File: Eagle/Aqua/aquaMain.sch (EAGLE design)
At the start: 41 parts, among them IC1 ATMEGA168-20P, IC2 DS1307, IC3 74HC125N, IC4 L7805CV, IC5 LF33CV, IC6 PCF8574P, IC7 24LC256P, IC8 40106N, J1 POWER_JACKSLT, T1 BC337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

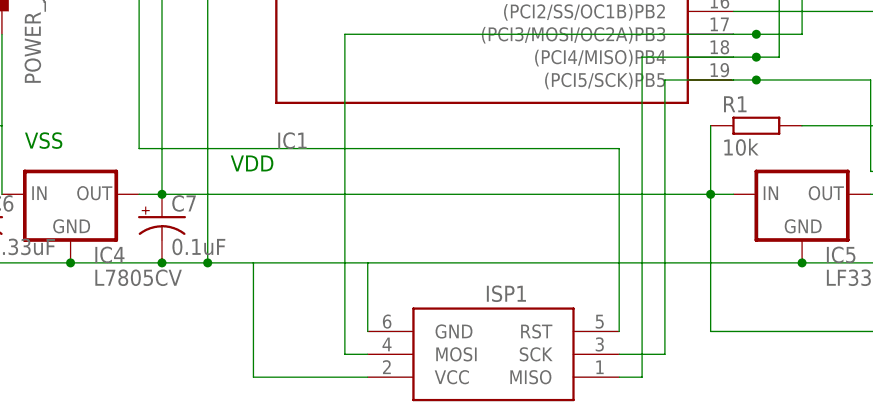
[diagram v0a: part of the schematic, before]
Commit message: Filled empty spaces with copper (faster eatching) Redone ArduinoNANO to DIP28 PCB to a single-side version Added V1 printout image
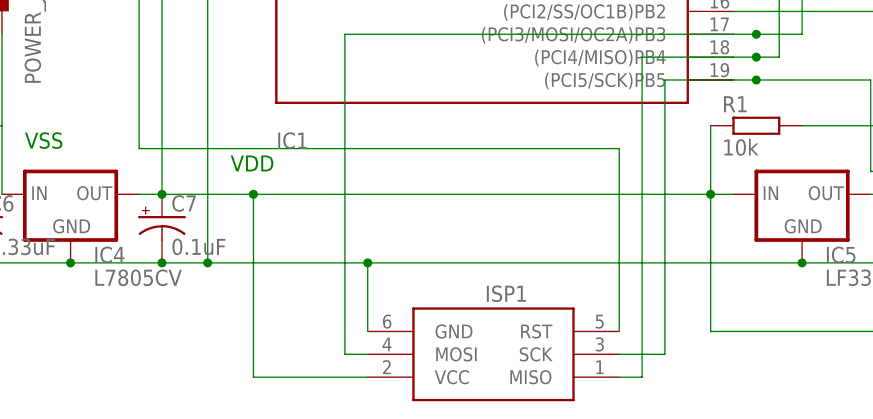
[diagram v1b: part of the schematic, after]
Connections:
- net N$25: now also ISP1.VCC
- net VSS: no longer ISP1.VCC
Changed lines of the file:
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@@
 <junction x="187.96" y="106.68"/>
 <pinref part="IC5" gate="G$1" pin="IN"/>
-<wire x1="68.58" y1="12.7" x2="129.54" y2="12.7" width="0.1524" layer="91"/>
+<wire x1="68.58" y1="12.7" x2="78.74" y2="12.7" width="0.1524" layer="91"/>
 <junction x="68.58" y="12.7"/>
 <pinref part="R1" gate="G$1" pin="1"/>
+<wire x1="78.74" y1="12.7" x2="129.54" y2="12.7" width="0.1524" layer="91"/>
 <wire x1="129.54" y1="12.7" x2="132.08" y2="12.7" width="0.1524" layer="91"/>
 <wire x1="129.54" y1="20.32" x2="129.54" y2="12.7" width="0.1524" layer="91"/>
@@
 <junction x="149.86" y="106.68"/>
 <pinref part="C7" gate="G$1" pin="+"/>
+<pinref part="ISP1" gate="G$1" pin="VCC"/>
+<wire x1="91.44" y1="-7.62" x2="78.74" y2="-7.62" width="0.1524" layer="91"/>
+<wire x1="78.74" y1="-7.62" x2="78.74" y2="12.7" width="0.1524" layer="91"/>
+<junction x="78.74" y="12.7"/>
 </segment>
 </net>
@@
 <wire x1="154.94" y1="5.08" x2="139.7" y2="5.08" width="0.1524" layer="91"/>
 <wire x1="139.7" y1="5.08" x2="91.44" y2="5.08" width="0.1524" layer="91"/>
-<wire x1="91.44" y1="5.08" x2="78.74" y2="5.08" width="0.1524" layer="91"/>
-<wire x1="78.74" y1="5.08" x2="73.66" y2="5.08" width="0.1524" layer="91"/>
+<wire x1="91.44" y1="5.08" x2="73.66" y2="5.08" width="0.1524" layer="91"/>
 <wire x1="203.2" y1="22.86" x2="203.2" y2="5.08" width="0.1524" layer="91"/>
 <junction x="203.2" y="5.08"/>
@@
 <pinref part="ISP1" gate="G$1" pin="GND"/>
 <wire x1="91.44" y1="-2.54" x2="91.44" y2="5.08" width="0.1524" layer="91"/>
-<pinref part="ISP1" gate="G$1" pin="VCC"/>
-<wire x1="91.44" y1="-7.62" x2="78.74" y2="-7.62" width="0.1524" layer="91"/>
-<wire x1="78.74" y1="-7.62" x2="78.74" y2="5.08" width="0.1524" layer="91"/>
 <pinref part="R4" gate="1" pin="1"/>
 <wire x1="91.44" y1="144.78" x2="91.44" y2="142.24" width="0.1524" layer="91"/>
@@
 <pinref part="C8" gate="G$1" pin="-"/>
 <junction x="154.94" y="5.08"/>
-</segment>
-</net>
+<junction x="91.44" y="5.08"/>
+</segment>
+</net>

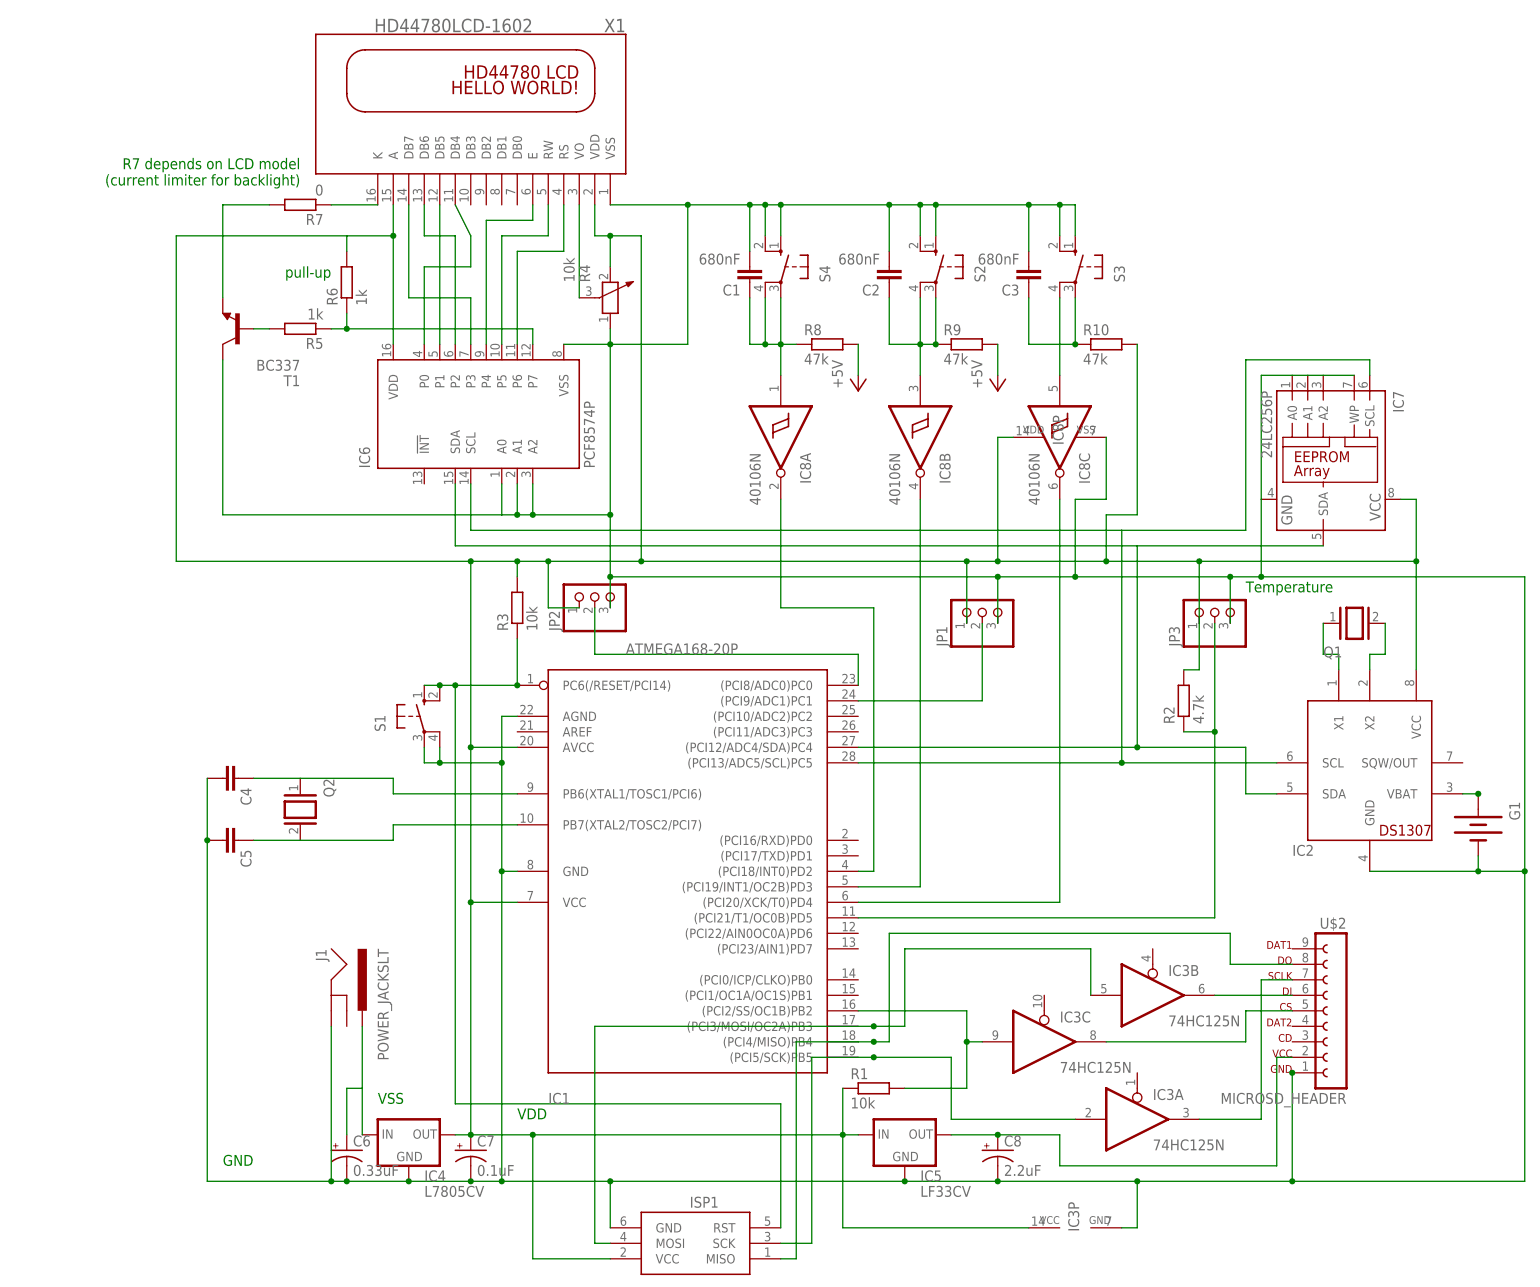
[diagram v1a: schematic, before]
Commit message: Big update Many important fixes dictated by 1st prototype
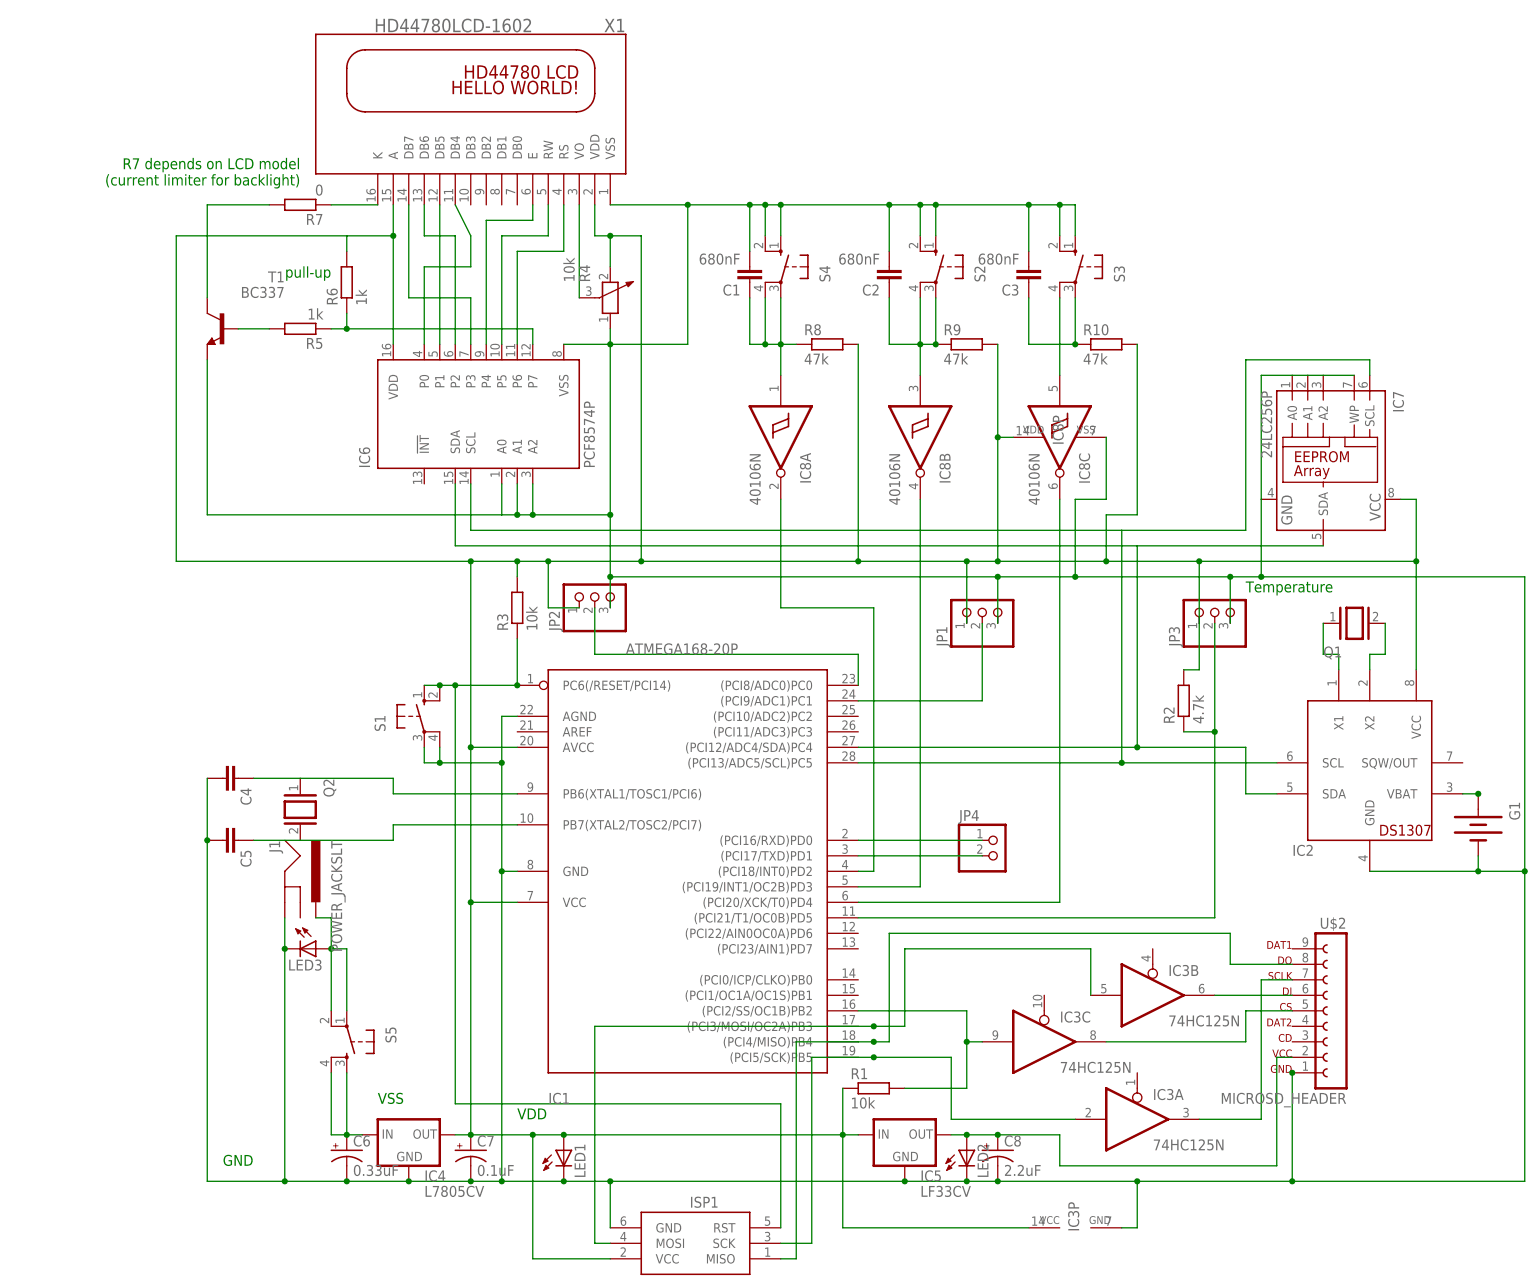
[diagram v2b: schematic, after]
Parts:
- added JP4: (no value), pinhead:PINHD-1X2
- added LED1, LED2, LED3: (no value), SparkFun-LED:LED3MM
- added S5: (no value), SparkFun-Electromechanical:TAC_SWITCHPTH
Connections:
- removed net +5V: R8.2, R9.2
- removed net N$1: C6.+, IC4.IN, J1.PWR
- new net N$31: J1.PWR, LED3.A, S5.1, S5.2
- new net N$46: C6.+, IC4.IN, S5.3, S5.4
- new net N$56: IC1.(PCI16/RXD)PD0, JP4.1
- new net N$57: IC1.(PCI17/TXD)PD1, JP4.2
- net N$22: now also LED2.A
- net N$25: now also LED1.A, R8.2, R9.2
- net N$42: now also T1.C; no longer T1.E
- net VSS: now also LED1.C, LED2.C, LED3.C, T1.E; no longer T1.C
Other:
- moved on the sheet: J1, T1

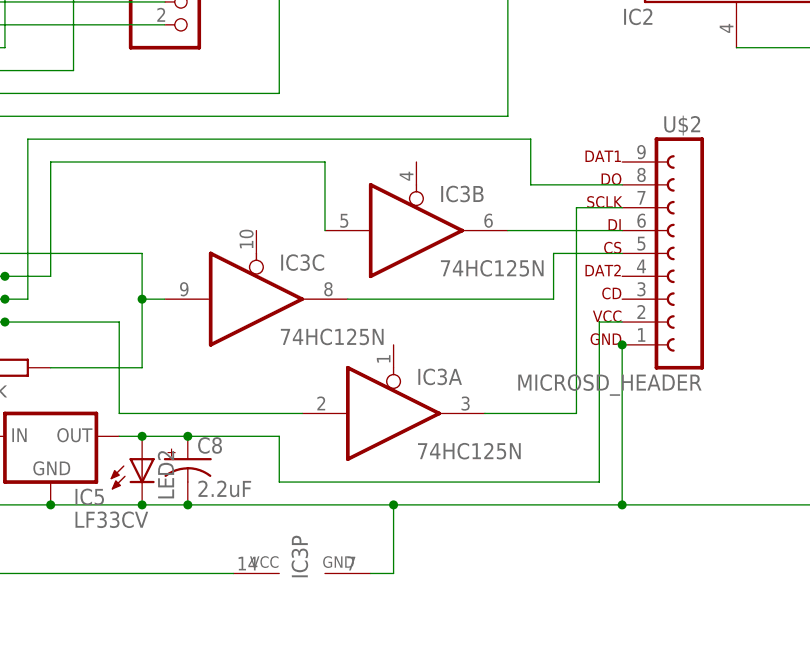
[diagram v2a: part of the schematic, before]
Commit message: - important fix to SD wiring (not implemented in PCB yet) - SD logging function in arduino project
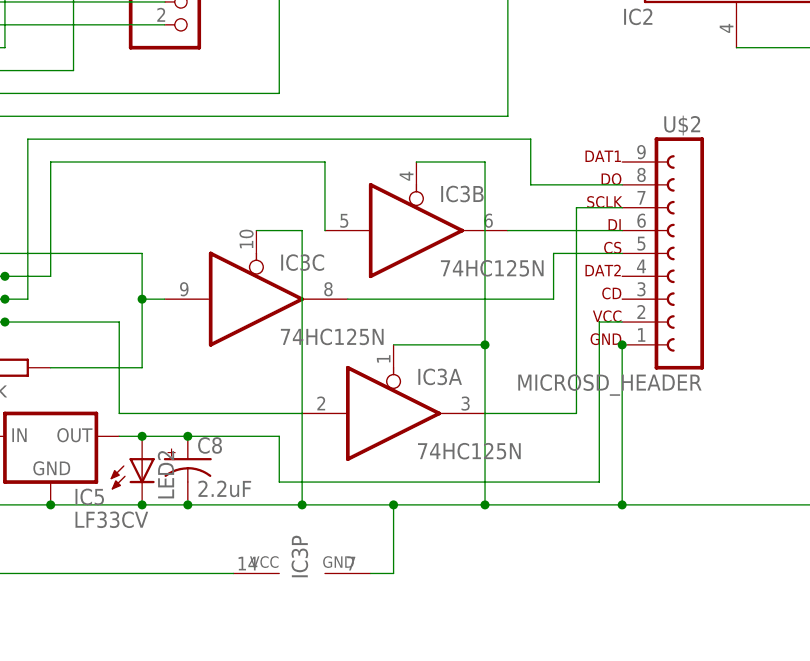
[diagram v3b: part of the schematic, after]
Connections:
- net VSS: now also IC3A.OE, IC3B.OE, IC3C.OE
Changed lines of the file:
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@@
 <junction x="73.66" y="5.08"/>
 <junction x="73.66" y="55.88"/>
-<wire x1="203.2" y1="5.08" x2="177.8" y2="5.08" width="0.1524" layer="91"/>
-<wire x1="177.8" y1="5.08" x2="154.94" y2="5.08" width="0.1524" layer="91"/>
+<wire x1="203.2" y1="5.08" x2="187.96" y2="5.08" width="0.1524" layer="91"/>
+<wire x1="187.96" y1="5.08" x2="177.8" y2="5.08" width="0.1524" layer="91"/>
+<wire x1="177.8" y1="5.08" x2="167.64" y2="5.08" width="0.1524" layer="91"/>
+<wire x1="167.64" y1="5.08" x2="154.94" y2="5.08" width="0.1524" layer="91"/>
 <wire x1="154.94" y1="5.08" x2="149.86" y2="5.08" width="0.1524" layer="91"/>
 <wire x1="149.86" y1="5.08" x2="139.7" y2="5.08" width="0.1524" layer="91"/>
@@
 <pinref part="T1" gate="G$1" pin="E"/>
 <wire x1="25.4" y1="139.7" x2="25.4" y2="114.3" width="0.1524" layer="91"/>
+<pinref part="IC3" gate="A" pin="OE"/>
+<wire x1="177.8" y1="22.86" x2="187.96" y2="22.86" width="0.1524" layer="91"/>
+<wire x1="187.96" y1="22.86" x2="187.96" y2="5.08" width="0.1524" layer="91"/>
+<pinref part="IC3" gate="B" pin="OE"/>
+<wire x1="180.34" y1="43.18" x2="187.96" y2="43.18" width="0.1524" layer="91"/>
+<wire x1="187.96" y1="43.18" x2="187.96" y2="22.86" width="0.1524" layer="91"/>
+<pinref part="IC3" gate="C" pin="OE"/>
+<wire x1="162.56" y1="35.56" x2="167.64" y2="35.56" width="0.1524" layer="91"/>
+<wire x1="167.64" y1="35.56" x2="167.64" y2="5.08" width="0.1524" layer="91"/>
+<junction x="167.64" y="5.08"/>
+<junction x="187.96" y="22.86"/>
+<junction x="187.96" y="5.08"/>
 </segment>
 </net>

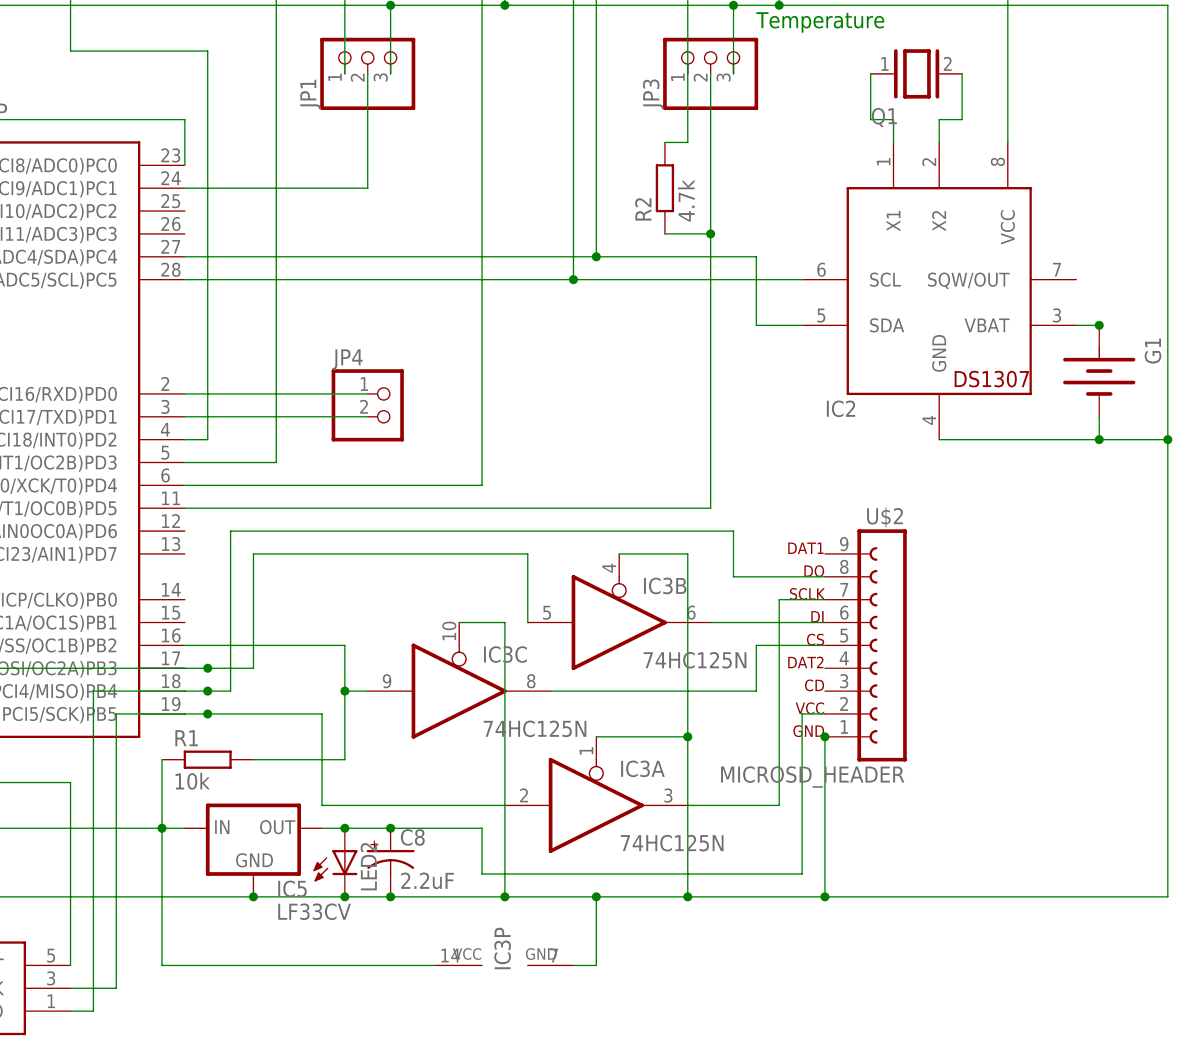
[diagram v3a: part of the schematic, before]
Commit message: Final project commit: - prototype proven to working continously for 4 months as of 1/8/15 - added pictures - [1/5/15] improvement - decrease R2 to 2.2kOhm, improved SNR from DS18B20 - project finished
Achieved:
- LCD display over i2c interface
- Functional 3-button menu English and Polish
- Ph probe reading with calibration code
- EEPROM save of Ph calibration
- Temperature reading [DS18B20]
- Data and clock [DS1307]
- SD card logging

Signed-off-by: pradyjowski <patryk.radyjowski@gmail.com>
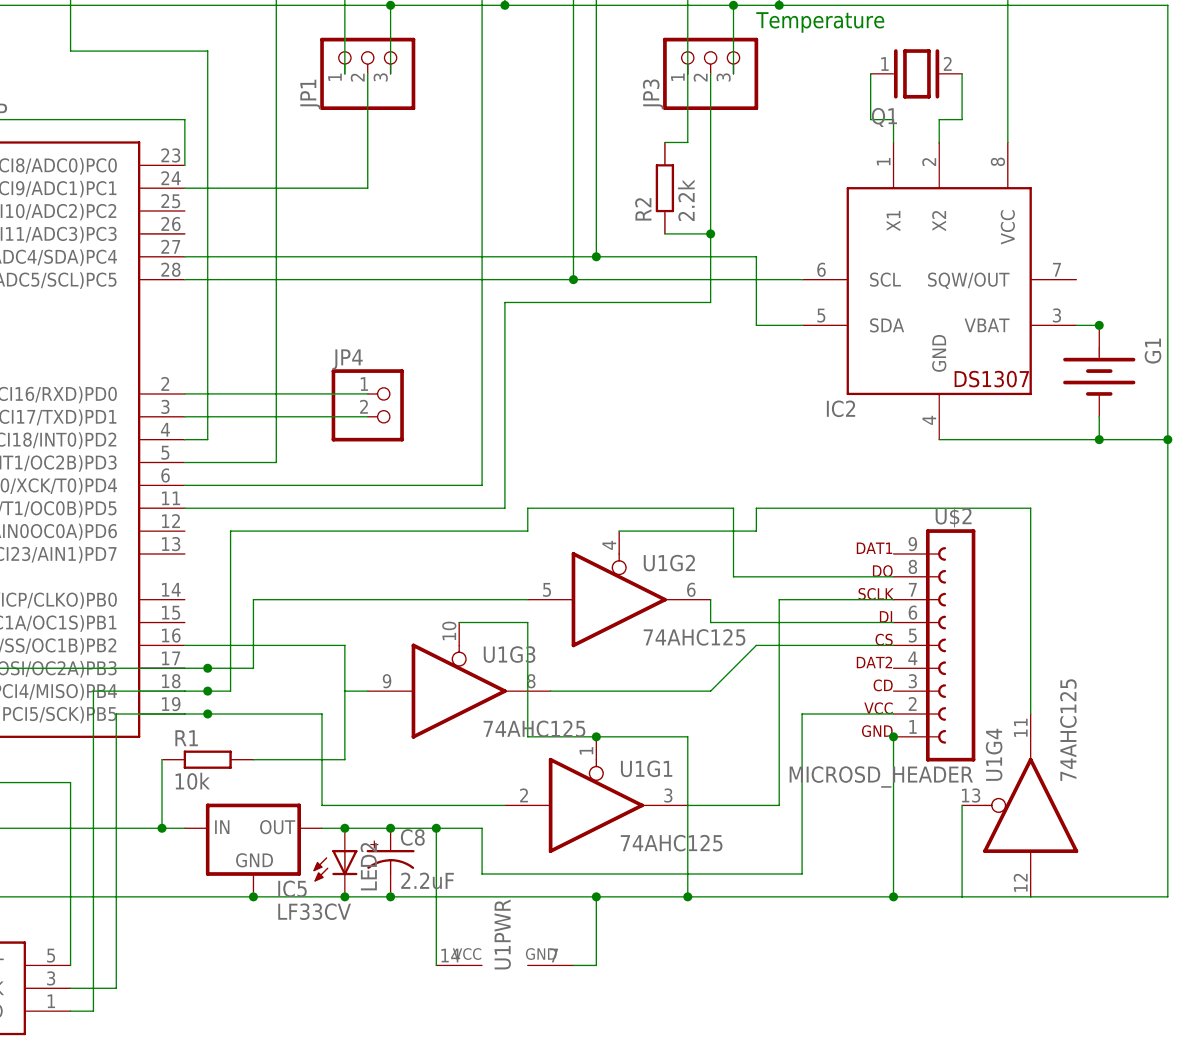
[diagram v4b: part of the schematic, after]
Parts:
- removed IC3: 74HC125N, 74xx-eu:74HC125N
- added U1: 74AHC125, dedicatedLib:74AHC125
- R2: value 4.7k -> 2.2k
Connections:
- new net N$58: U1G2.OE, U1G4.O
- net N$14: now also U1G2.I; no longer IC3B.I
- net N$15: now also IC1.(PCI2/SS/OC1B)PB2, R1.2, U1G3.I; no longer IC3B.O, U$2.6
- net N$16: now also U1G1.I; no longer IC3A.I
- net N$17: now also U1G1.O; no longer IC3A.O
- net N$18: now also U$2.5, U1G3.O; no longer IC1.(PCI2/SS/OC1B)PB2, IC3C.I, R1.2
- net N$19: now also U$2.6, U1G2.O; no longer IC3C.O, U$2.5
- net N$22: now also U1PWR.VCC
- net N$25: no longer IC3P.VCC
- net VSS: now also U1G1.OE, U1G3.OE, U1G4.I, U1G4.OE, U1PWR.GND; no longer IC3A.OE, IC3B.OE, IC3C.OE, IC3P.GND
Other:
- moved on the sheet: U$2
